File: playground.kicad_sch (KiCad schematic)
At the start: 50 parts, among them IC11 LM3940IMP-3.3_NOPB, IC9 L293DD, J1 67643-2910, J2 Pump, J3 Fan, J4 Valve, J5 Conn_02x05_Counter_Clockwise, J6 MOLEX POWER CONNECTOR, U2 ATSAMD21G18A-A, Y1 32.768kHz

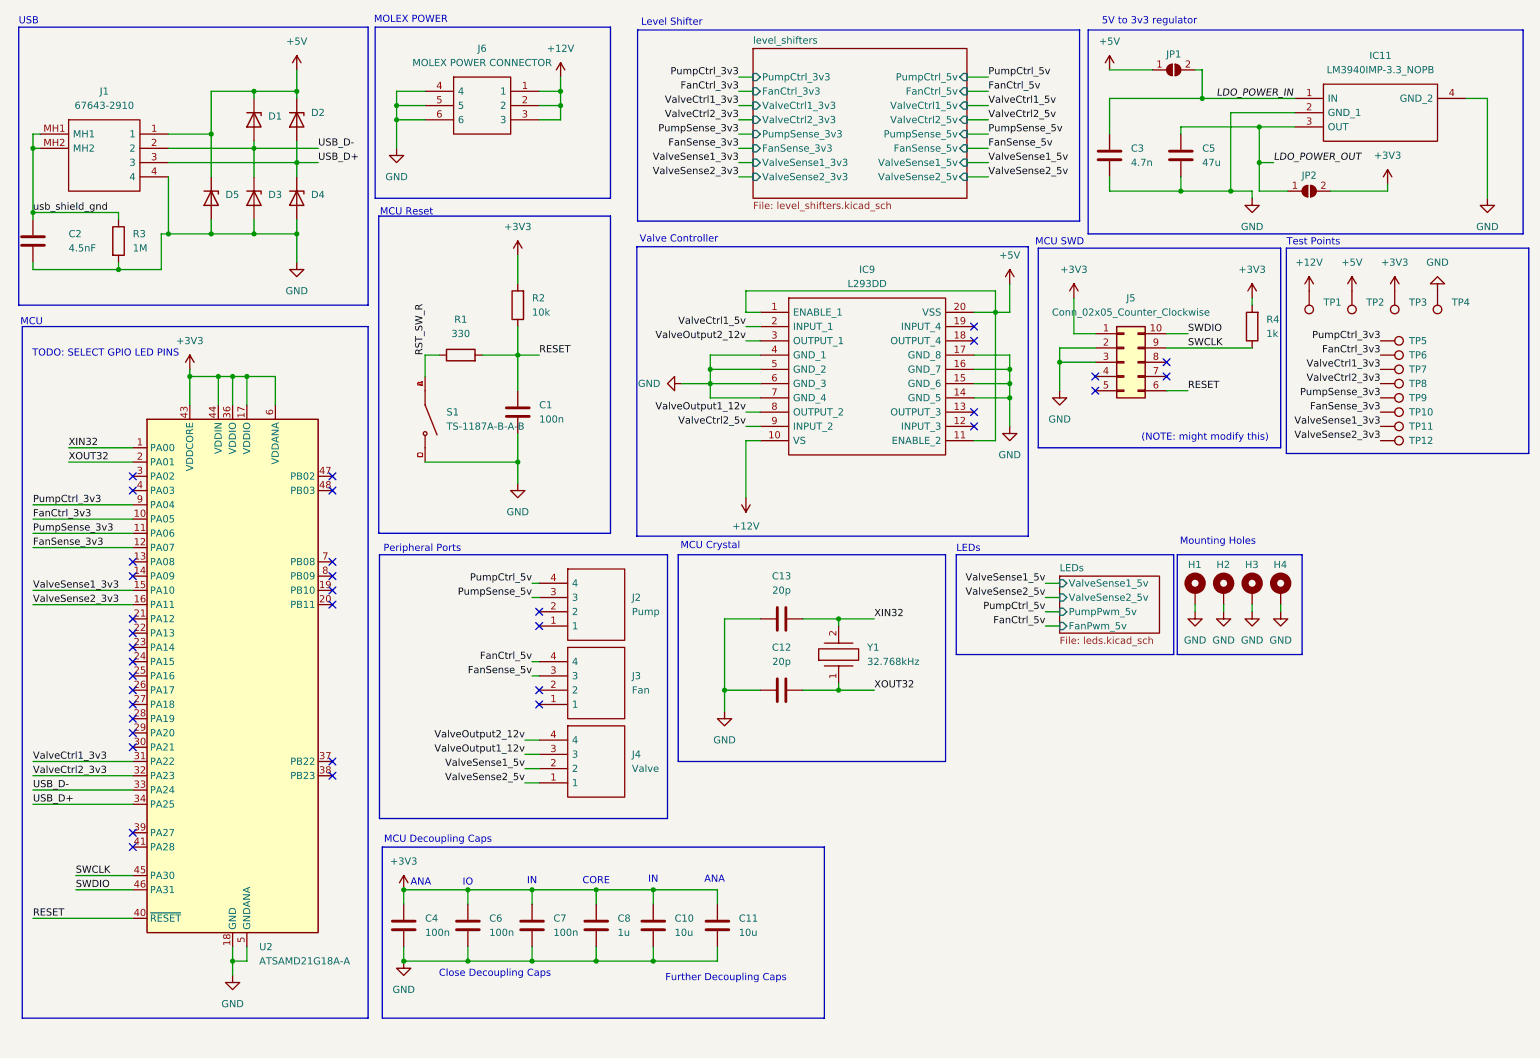
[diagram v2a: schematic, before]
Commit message: Small part substitutions. Working on BOM
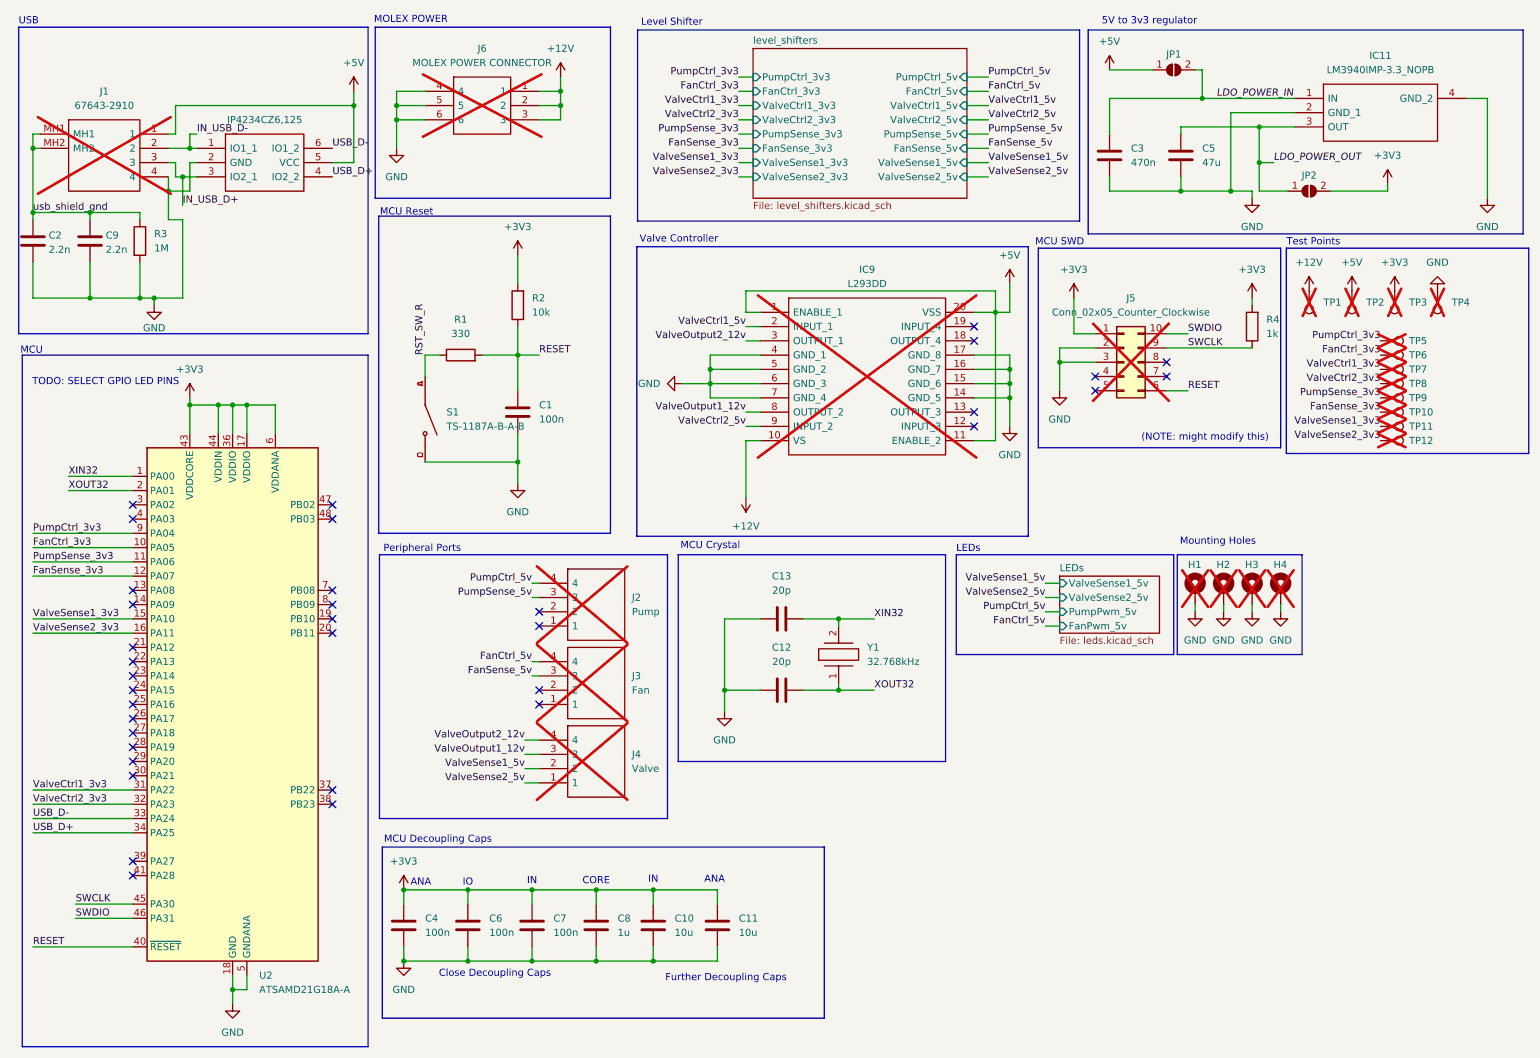
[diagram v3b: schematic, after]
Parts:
- removed D1, D3, D4, D5: ~, Diode_SMD:D_0805_2012Metric, symbol Device:D_Zener
- removed D2: D_Zener, Diode_SMD:D_0805_2012Metric, symbol Device:D_Zener
- added C9: 2.2n, Capacitor_SMD:C_0805_2012Metric, symbol Device:C
- added D1: IP4234CZ6,125, custom_footprints:SOP95P275X110-6N, symbol custom_symbols:IP4234CZ6,125
- C1, C4, C6, C7: LCSC (none) -> C49678
- C10, C11: LCSC (none) -> C15850
- C12, C13: LCSC (none) -> C105173
- C2: value 4.5nF -> 2.2n; LCSC (none) -> C28260
- C3: value 4.7n -> 470n; LCSC (none) -> C13967
- C5: LCSC (none) -> C16780
- C8: LCSC (none) -> C307362
- H1, H2, H3, H4, IC9, J1, J2, J3, J4, J5, J6, TP1, TP10, TP11, TP12, TP2, TP3, TP4, TP5, TP6, TP7, TP8, TP9: now not fitted; now left out of the parts list
- IC11: LCSC (none) -> LM3940IMP-3.3/NOPB
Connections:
- net +5V: now also D1.5 (VCC)
- net GND: now also C9.2, D1.2 (GND)
- net USB_D+: now also D1.4 (IO2_2); no longer J1.3
- net USB_D-: now also D1.6 (IO1_2); no longer J1.2
- net usb_shield_gnd: now also C9.1
- new net IN_USB_D+: D1.3 (IO2_1), J1.3
- new net IN_USB_D-: D1.1 (IO1_1), J1.2
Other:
- moved on the sheet: R3, U2

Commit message: Added all part numbers
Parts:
- R1: LCSC (none) -> C17630
- R2: LCSC (none) -> C17414
- R3: LCSC (none) -> C17514
- R4: LCSC (none) -> C17513
- S1: LCSC (none) -> C318884
- U2: LCSC (none) -> C78624
- Y1: LCSC (none) -> C32346
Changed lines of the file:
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@@
 			)
 		)
+		(property "LCSC" "C78624"
+			(at 53.34 135.89 0)
+			(effects
+				(font
+					(size 1.27 1.27)
+				)
+				(hide yes)
+			)
+		)
 		(pin "13"
 		)
@@
 			)
 		)
+		(property "LCSC" "C32346"
+			(at 161.29 132.08 0)
+			(effects
+				(font
+					(size 1.27 1.27)
+				)
+				(hide yes)
+			)
+		)
 		(pin "2"
 		)
@@
 			)
 		)
+		(property "LCSC" "C17630"
+			(at 93.98 73.66 0)
+			(effects
+				(font
+					(size 1.27 1.27)
+				)
+				(hide yes)
+			)
+		)
 		(pin "2"
 		)
@@
 			)
 		)
+		(property "LCSC" "C318884"
+			(at 87.63 85.09 0)
+			(effects
+				(font
+					(size 1.27 1.27)
+				)
+				(hide yes)
+			)
+		)
 		(pin "D"
 		)
@@
 			)
 		)
+		(property "LCSC" "C17513"
+			(at 234.95 68.58 0)
+			(effects
+				(font
+					(size 1.27 1.27)
+				)
+				(hide yes)
+			)
+		)
 		(pin "2"
 		)
@@
 			)
 		)
+		(property "LCSC" "C17414"
+			(at 104.14 64.77 0)
+			(effects
+				(font
+					(size 1.27 1.27)
+				)
+				(hide yes)
+			)
+		)
 		(pin "2"
 		)
@@
 			(at 36.83 53.34 0)
 			(effects
+				(font
+					(size 1.27 1.27)
+				)
+				(hide yes)
+			)
+		)
+		(property "LCSC" "C17514"
+			(at 36.83 53.34 0)
+			(effects

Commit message: Prepped for production.
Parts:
- IC11: LCSC LM3940IMP-3.3/NOPB -> C140319
- JP1, JP2: now not fitted; now left out of the parts list
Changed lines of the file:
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@@
 		(unit 1)
 		(exclude_from_sim no)
-		(in_bom yes)
+		(in_bom no)
 		(on_board yes)
-		(dnp no)
+		(dnp yes)
 		(property "Reference" "JP1"
 			(at 220.98 20.066 0)
@@
 			)
 		)
-		(property "LCSC" "LM3940IMP-3.3/NOPB"
+		(property "LCSC" "C140319"
 			(at 242.57 27.94 0)
 			(effects
@@
 		(unit 1)
 		(exclude_from_sim no)
-		(in_bom yes)
+		(in_bom no)
 		(on_board yes)
-		(dnp no)
+		(dnp yes)
 		(property "Reference" "JP2"
 			(at 245.11 41.656 0)
